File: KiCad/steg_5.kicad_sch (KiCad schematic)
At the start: 12 parts, among them U1 W65C02S, U2 LCD-016N002L

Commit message: Kicad projekt ligger här nu, med alla steg
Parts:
- removed A1: Arduino_Mega2560_R3_Shield, PCM_arduino-library:Arduino_Mega2560_R3_Shield, symbol arduino-library:Arduino_Mega2560_R3_Shield
- removed R1, R2, R3, R4, R5, R6, R7: (no value), symbol Device:R_US
- removed U1: W65C02S, Package_DIP:DIP-40_W15.24mm, symbol 65xx-library:W65C02SxP
- removed U2: LCD-016N002L, Display:LCD-016N002L, symbol Display_Character:LCD-016N002L
- added A3: Mega2560, PCM_arduino-library:Arduino_Mega2560_R3_Shield, symbol arduino-library:Arduino_Mega2560_R3_Shield
- added C5: 100nF, symbol Device:C_Small
- added R15, R16, R17, R18, R19, R20, R21: (no value), symbol Device:R_US
- added U7: W65C02S, Package_DIP:DIP-40_W15.24mm, symbol 65xx-library:W65C02SxP
- added U8: LCD, Display:LCD-016N002L, symbol Display_Character:LCD-016N002L
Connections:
- net +5V: now also C5.1, R15.1, R16.1, R17.1, R18.1, R19.1, R21.1, U7.8 (VDD), U8.2 (VDD)
- net A0: now also A3.A0, U7.9 (A0)
- net A1: now also A3.A1, U7.10 (A1)
- net A10: now also A3.A10, U7.19 (A10)
- net A11: now also A3.A11, U7.20 (A11)
- net A12: now also A3.A12, U7.22 (A12)
- net A13: now also A3.A13, U7.23 (A13)
- net A14: now also A3.A14, U7.24 (A14)
- net A15: now also A3.A15, U7.25 (A15)
- net A2: now also A3.A2, U7.11 (A2)
- net A3: now also A3.A3, U7.12 (A3)
- net A4: now also A3.A4, U7.13 (A4)
- net A5: now also A3.A5, U7.14 (A5)
- net A6: now also A3.A6, U7.15 (A6)
- net A7: now also A3.A7, U7.16 (A7)
- net A8: now also A3.A8, U7.17 (A8)
- net A9: now also A3.A9, U7.18 (A9)
- net D0: now also A3.D22, U7.33 (D0)
- net D1: now also A3.D23, U7.32 (D1)
- net D2: now also A3.D24, U7.31 (D2)
- net D3: now also A3.D25, U7.30 (D3)
- net D4: now also A3.D26, U7.29 (D4)
- net D5: now also A3.D27, U7.28 (D5)
- net D6: now also A3.D28, U7.27 (D6)
- net D7: now also A3.D29, U7.26 (D7)
- net DB4: now also A3.D10, U8.11 (DB4)
- net DB5: now also A3.D9, U8.12 (DB5)
- net DB6: now also A3.D8, U8.13 (DB6)
- net DB7: now also A3.D7, U8.14 (DB7)
- net Earth: now also A3.GND6 (GND), C5.2, R20.2, U7.21 (VSS), U8.1 (VSS), U8.16 (K), U8.5 (R/~{W})
- net at BTN1.1: now also A3.D11
- net at BTN2.1: now also A3.D12
- new net: R16.2, U7.36 (BE)
- new net: A3.D13, U7.7 (SYNC)
- new net: A3.D2 (D2_INT0), U7.37 (ϕ0)
- new net: A3.D3 (D3_INT1), U7.34 (R/~{W})
- new net: A3.D4, U7.40 (~{RES})
- new net: A3.D5, U8.4 (RS)
- new net: A3.D6, U8.6 (E)
- new net: R21.2, U8.15 (A/VEE)
- new net: R20.1, U8.3 (VO)
- new net: R17.2, U7.2 (RDY)
- new net: R18.2, U7.6 (~{NMI})
- new net: R15.2, U7.38 (~{SO})
- new net: R19.2, U7.4 (~{IRQ})

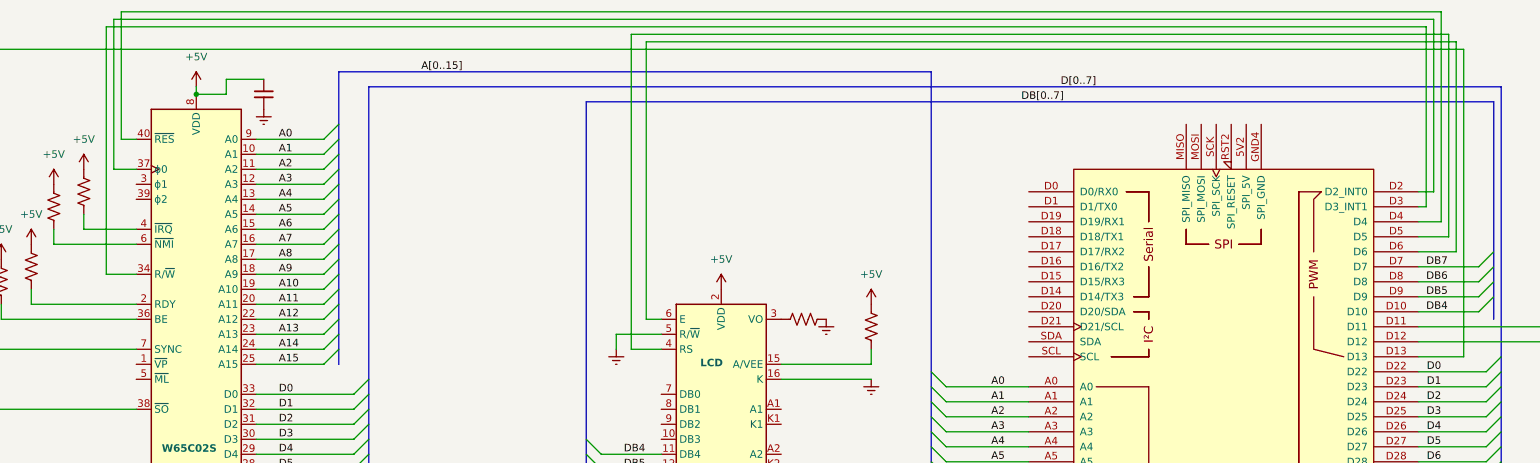
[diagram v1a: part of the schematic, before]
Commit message: Add trim potentiometer symbol and update power symbols in schematics
- Introduced a new trim potentiometer symbol (Device:R_Potentiometer_Trim) with properties for reference, value, footprint, and simulation details.
- Updated existing power symbols for +5V and Earth, including new references and descriptions.
- Adjusted positions and properties of various components in the schematic to enhance clarity and organization.
- Updated multiple schematic images to reflect the latest changes.
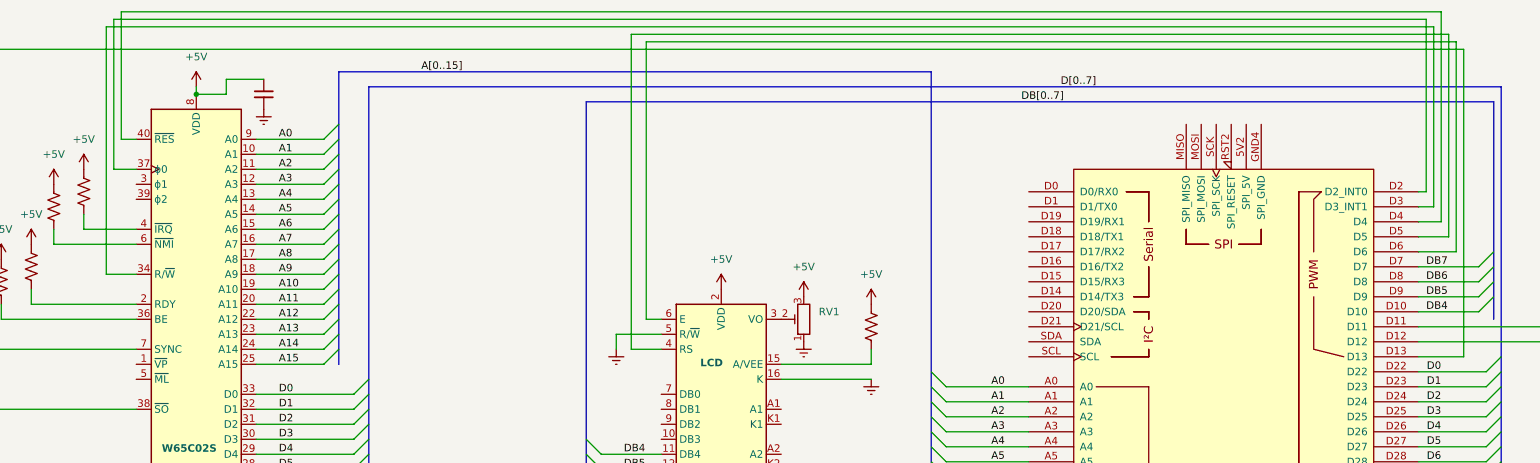
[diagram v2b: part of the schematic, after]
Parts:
- removed R20: (no value), symbol Device:R_US
- added RV1: R_Potentiometer_Trim, symbol Device:R_Potentiometer_Trim
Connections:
- net +5V: now also RV1.3
- net Earth: now also RV1.1
- net at U8.3 (VO): now also RV1.2
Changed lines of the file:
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@@
 	(wire
 		(pts
-			(xy 106.68 67.31) (xy 330.2 67.31)
+			(xy 106.68 67.31) (xy 331.47 67.31)
 		)
 		(stroke
@@
 	(wire
 		(pts
-			(xy 331.47 66.04) (xy 331.47 95.25)
+			(xy 330.2 66.04) (xy 330.2 95.25)
 		)
 		(stroke
@@
 	(wire
 		(pts
-			(xy 331.47 95.25) (xy 328.93 95.25)
+			(xy 330.2 95.25) (xy 328.93 95.25)
 		)
 		(stroke
@@
 	(wire
 		(pts
-			(xy 330.2 97.79) (xy 328.93 97.79)
+			(xy 331.47 97.79) (xy 328.93 97.79)
 		)
 		(stroke
@@
 	(wire
 		(pts
-			(xy 330.2 67.31) (xy 330.2 97.79)
+			(xy 331.47 67.31) (xy 331.47 97.79)
 		)
 		(stroke
@@
 	(wire
 		(pts
-			(xy 107.95 66.04) (xy 331.47 66.04)
+			(xy 107.95 66.04) (xy 330.2 66.04)
 		)
 		(stroke
@@
 	)
 	(symbol
+		(lib_id "power:+5V")
+		(at 224.79 113.03 0)
+		(unit 1)
+		(body_style 1)
+		(exclude_from_sim no)
+		(in_bom yes)
+		(on_board yes)
+		(in_pos_files yes)
+		(dnp no)
+		(fields_autoplaced yes)
+		(property "Reference" "#PWR058"
+			(at 224.79 116.84 0)
+			(hide yes)
+			(show_name no)
+			(do_not_autoplace no)
+			(effects
+				(font
+					(size 1.27 1.27)
+				)
+			)
+		)
+		(property "Value" "+5V"
+			(at 224.79 107.95 0)
+			(show_name no)
+			(do_not_autoplace no)
+			(effects
+				(font
+					(size 1.27 1.27)
+				)
+			)
+		)
+		(property "Footprint" ""
+			(at 224.79 113.03 0)
+			(hide yes)
+			(show_name no)
+			(do_not_autoplace no)
+			(effects
+				(font
+					(size 1.27 1.27)
+				)
+			)
+		)
+		(property "Datasheet" ""
+			(at 224.79 113.03 0)
+			(hide yes)
+			(show_name no)
+			(do_not_autoplace no)
+			(effects
+				(font
+					(size 1.27 1.27)
+				)
+			)
+		)
+		(property "Description" "Power symbol creates a global label with name \"+5V\""
+			(at 224.79 113.03 0)
+			(hide yes)
+			(show_name no)
+			(do_not_autoplace no)
+			(effects
+				(font
+					(size 1.27 1.27)
+				)
+			)
+		)
+		(pin "1"
+		)
+		(instances
+			(project "6502.smutje.se"
+				(path "/34693de8-e0e2-47e7-9988-a0d185b88162"
+					(reference "#PWR058")
+					(unit 1)
+				)
+			)
+		)
+	)
+	(symbol
 		(lib_id "Device:R_US")
 		(at 88.9 110.49 0)
@@
 	)
 	(symbol
+		(lib_id "power:Earth")
+		(at 224.79 120.65 0)
+		(unit 1)
+		(body_style 1)
+		(exclude_from_sim no)
+		(in_bom yes)
+		(on_board yes)
+		(in_pos_files yes)
+		(dnp no)
+		(fields_autoplaced yes)
+		(property "Reference" "#PWR057"
+			(at 224.79 127 0)
+			(hide yes)
+			(show_name no)
+			(do_not_autoplace no)
+			(effects
+				(font
+					(size 1.27 1.27)
+				)
+			)
+		)
+		(property "Value" "Earth"
+			(at 224.79 125.73 0)
+			(hide yes)
+			(show_name no)
+			(do_not_autoplace no)
+			(effects
+				(font
+					(size 1.27 1.27)
+				)
+			)
+		)
+		(property "Footprint" ""
+			(at 224.79 120.65 0)
+			(hide yes)
+			(show_name no)
+			(do_not_autoplace no)
+			(effects
+				(font
+					(size 1.27 1.27)
+				)
+			)
+		)
+		(property "Datasheet" ""
+			(at 224.79 120.65 0)
+			(hide yes)
+			(show_name no)
+			(do_not_autoplace no)
+			(effects
+				(font
+					(size 1.27 1.27)
+				)
+			)
+		)
+		(property "Description" "Power symbol creates a global label with name \"Earth\""
+			(at 224.79 120.65 0)
+			(hide yes)
+			(show_name no)
+			(do_not_autoplace no)
+			(effects
+				(font
+					(size 1.27 1.27)
+				)
+			)
+		)
+		(pin "1"
+		)
+		(instances
+			(project "6502.smutje.se"
+				(path "/34693de8-e0e2-47e7-9988-a0d185b88162"
+					(reference "#PWR057")
+					(unit 1)
+				)
+			)
+		)
+	)
+	(symbol
 		(lib_id "Device:R_US")
 		(at 97.79 97.79 0)
@@
 	)
 	(symbol
-		(lib_id "power:Earth")
-		(at 228.6 116.84 0)
+		(lib_id "Device:R_Potentiometer_Trim")
+		(at 224.79 116.84 180)
 		(unit 1)
 		(body_style 1)
@@
 		(dnp no)
 		(fields_autoplaced yes)
-		(property "Reference" "#PWR049"
-			(at 228.6 123.19 0)
-			(hide yes)
+		(property "Reference" "RV1"
+			(at 227.33 115.5699 0)
 			(show_name no)
 			(do_not_autoplace no)
@@
 					(size 1.27 1.27)
 				)
+				(justify right)
 			)
 		)
-		(property "Value" "Earth"
-			(at 228.6 121.92 0)
+		(property "Value" "R_Potentiometer_Trim"
+			(at 227.33 118.1099 0)
 			(hide yes)
 			(show_name no)
@@
 					(size 1.27 1.27)
 				)
+				(justify right)
 			)
 		)
 		(property "Footprint" ""
-			(at 228.6 116.84 0)
+			(at 224.79 116.84 0)
 			(hide yes)
 			(show_name no)
@@
 		)
 		(property "Datasheet" ""
-			(at 228.6 116.84 0)
+			(at 224.79 116.84 0)
 			(hide yes)
 			(show_name no)
@@
 			)
 		)
-		(property "Description" "Power symbol creates a global label with name \"Earth\""
-			(at 228.6 116.84 0)
+		(property "Description" "Trim-potentiometer"
+			(at 224.79 116.84 0)
+			(hide yes)
+			(show_name no)
+			(do_not_autoplace no)
+			(effects
+				(font
+					(size 1.27 1.27)
+				)
+			)
+		)
+		(property "Sim.Device" "R"
+			(at 224.79 116.84 0)
 			(hide yes)
 			(show_name no)
@@
 			)
 		)
+		(property "Sim.Type" "POT"
+			(at 224.79 116.84 0)
+			(hide yes)
+			(show_name no)
+			(do_not_autoplace no)
+			(effects
+				(font
+					(size 1.27 1.27)
+				)
+			)
+		)
+		(property "Sim.Pins" "1=r0 2=wiper 3=r1"
+			(at 224.79 116.84 0)
+			(hide yes)
+			(show_name no)
+			(do_not_autoplace no)
+			(effects
+				(font
+					(size 1.27 1.27)
+				)
+			)
+		)
+		(pin "3"
+		)
+		(pin "2"
+		)
 		(pin "1"
 		)
@@
 			(project "6502.smutje.se"
 				(path "/34693de8-e0e2-47e7-9988-a0d185b88162"
-					(reference "#PWR049")
+					(reference "RV1")
 					(unit 1)
 				)
@@
 					(unit 1)
 				)
-			)
-		)
-	)
-	(symbol
-		(lib_id "Device:R_US")
-		(at 224.79 116.84 90)
-		(unit 1)
-		(body_style 1)
-		(exclude_from_sim no)
-		(in_bom yes)
-		(on_board yes)
-		(in_pos_files yes)
-		(dnp no)
-		(property "Reference" "R20"
-			(at 223.5199 114.3 90)
-			(hide yes)
-			(show_name no)
-			(do_not_autoplace no)
-			(effects
-				(font
-					(size 1.27 1.27)
-				)
-				(justify left)
-			)
-		)
-		(property "Value" ""
-			(at 226.0599 114.3 0)
-			(show_name no)
-			(do_not_autoplace no)
-			(effects
-				(font
-					(size 1.27 1.27)
-				)
-				(justify left)
-			)
-		)
-		(property "Footprint" ""
-			(at 225.044 115.824 90)
-			(hide yes)
-			(show_name no)
-			(do_not_autoplace no)
-			(effects
-				(font
-					(size 1.27 1.27)
-				)
-			)
-		)
-		(property "Datasheet" ""
-			(at 224.79 116.84 0)
-			(hide yes)
-			(show_name no)
-			(do_not_autoplace no)
-			(effects
-				(font
-					(size 1.27 1.27)
-				)
-			)
-		)
-		(property "Description" "Resistor, US symbol"
-			(at 224.79 116.84 0)
-			(hide yes)
-			(show_name no)
-			(do_not_autoplace no)
-			(effects
-				(font
-					(size 1.27 1.27)
-				)
-			)
-		)
-		(pin "1"
-		)
-		(pin "2"
-		)
-		(instances
-			(project "6502.smutje.se"
-				(path "/34693de8-e0e2-47e7-9988-a0d185b88162"
-					(reference "R20")
-					(unit 1)
-				)

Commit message: Revert "Add trim potentiometer symbol and update power symbols in schematics"
This reverts commit c4bb345892a428583a00d61d4c040ffcc3a1eb40.
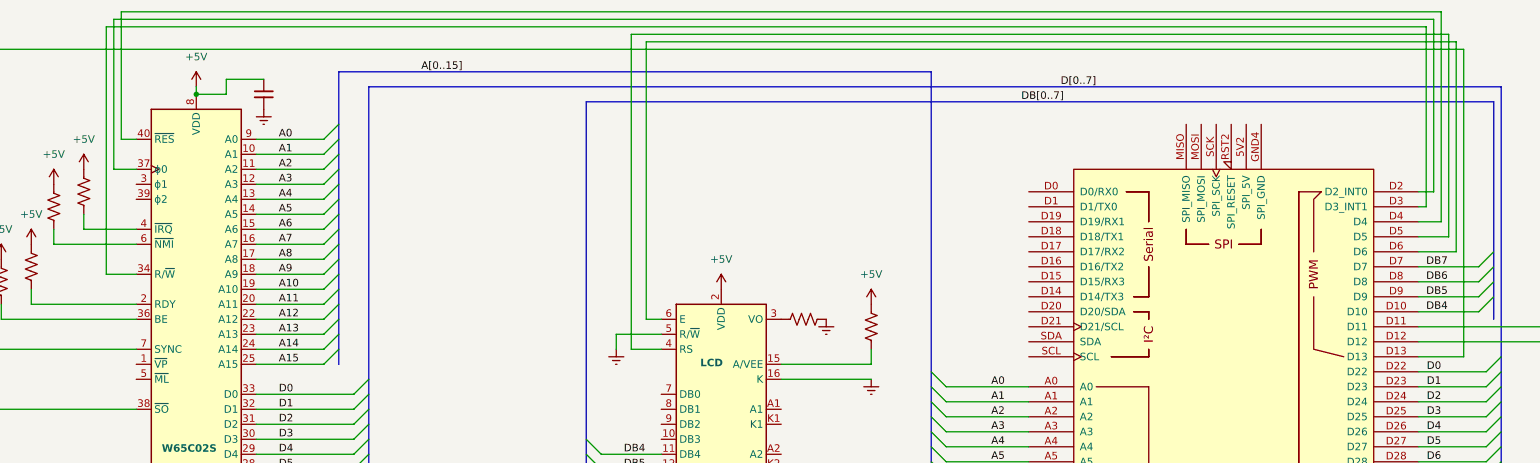
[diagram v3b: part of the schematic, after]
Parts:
- removed RV1: R_Potentiometer_Trim, symbol Device:R_Potentiometer_Trim
- added R20: (no value), symbol Device:R_US
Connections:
- net Earth: now also R20.2
- net at U8.3 (VO): now also R20.1
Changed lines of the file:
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@@
 	(wire
 		(pts
-			(xy 106.68 67.31) (xy 331.47 67.31)
+			(xy 106.68 67.31) (xy 330.2 67.31)
 		)
 		(stroke
@@
 	(wire
 		(pts
-			(xy 330.2 66.04) (xy 330.2 95.25)
+			(xy 331.47 66.04) (xy 331.47 95.25)
 		)
 		(stroke
@@
 	(wire
 		(pts
-			(xy 330.2 95.25) (xy 328.93 95.25)
+			(xy 331.47 95.25) (xy 328.93 95.25)
 		)
 		(stroke
@@
 	(wire
 		(pts
-			(xy 331.47 97.79) (xy 328.93 97.79)
+			(xy 330.2 97.79) (xy 328.93 97.79)
 		)
 		(stroke
@@
 	(wire
 		(pts
-			(xy 331.47 67.31) (xy 331.47 97.79)
+			(xy 330.2 67.31) (xy 330.2 97.79)
 		)
 		(stroke
@@
 	(wire
 		(pts
-			(xy 107.95 66.04) (xy 330.2 66.04)
+			(xy 107.95 66.04) (xy 331.47 66.04)
 		)
 		(stroke
@@
 	)
 	(symbol
-		(lib_id "power:+5V")
-		(at 224.79 113.03 0)
-		(unit 1)
-		(body_style 1)
-		(exclude_from_sim no)
-		(in_bom yes)
-		(on_board yes)
-		(in_pos_files yes)
-		(dnp no)
-		(fields_autoplaced yes)
-		(property "Reference" "#PWR058"
-			(at 224.79 116.84 0)
-			(hide yes)
-			(show_name no)
-			(do_not_autoplace no)
-			(effects
-				(font
-					(size 1.27 1.27)
-				)
-			)
-		)
-		(property "Value" "+5V"
-			(at 224.79 107.95 0)
-			(show_name no)
-			(do_not_autoplace no)
-			(effects
-				(font
-					(size 1.27 1.27)
-				)
-			)
-		)
-		(property "Footprint" ""
-			(at 224.79 113.03 0)
-			(hide yes)
-			(show_name no)
-			(do_not_autoplace no)
-			(effects
-				(font
-					(size 1.27 1.27)
-				)
-			)
-		)
-		(property "Datasheet" ""
-			(at 224.79 113.03 0)
-			(hide yes)
-			(show_name no)
-			(do_not_autoplace no)
-			(effects
-				(font
-					(size 1.27 1.27)
-				)
-			)
-		)
-		(property "Description" "Power symbol creates a global label with name \"+5V\""
-			(at 224.79 113.03 0)
-			(hide yes)
-			(show_name no)
-			(do_not_autoplace no)
-			(effects
-				(font
-					(size 1.27 1.27)
-				)
-			)
-		)
-		(pin "1"
-		)
-		(instances
-			(project "6502.smutje.se"
-				(path "/34693de8-e0e2-47e7-9988-a0d185b88162"
-					(reference "#PWR058")
-					(unit 1)
-				)
-			)
-		)
-	)
-	(symbol
 		(lib_id "Device:R_US")
 		(at 88.9 110.49 0)
@@
 	)
 	(symbol
-		(lib_id "power:Earth")
-		(at 224.79 120.65 0)
-		(unit 1)
-		(body_style 1)
-		(exclude_from_sim no)
-		(in_bom yes)
-		(on_board yes)
-		(in_pos_files yes)
-		(dnp no)
-		(fields_autoplaced yes)
-		(property "Reference" "#PWR057"
-			(at 224.79 127 0)
-			(hide yes)
-			(show_name no)
-			(do_not_autoplace no)
-			(effects
-				(font
-					(size 1.27 1.27)
-				)
-			)
-		)
-		(property "Value" "Earth"
-			(at 224.79 125.73 0)
-			(hide yes)
-			(show_name no)
-			(do_not_autoplace no)
-			(effects
-				(font
-					(size 1.27 1.27)
-				)
-			)
-		)
-		(property "Footprint" ""
-			(at 224.79 120.65 0)
-			(hide yes)
-			(show_name no)
-			(do_not_autoplace no)
-			(effects
-				(font
-					(size 1.27 1.27)
-				)
-			)
-		)
-		(property "Datasheet" ""
-			(at 224.79 120.65 0)
-			(hide yes)
-			(show_name no)
-			(do_not_autoplace no)
-			(effects
-				(font
-					(size 1.27 1.27)
-				)
-			)
-		)
-		(property "Description" "Power symbol creates a global label with name \"Earth\""
-			(at 224.79 120.65 0)
-			(hide yes)
-			(show_name no)
-			(do_not_autoplace no)
-			(effects
-				(font
-					(size 1.27 1.27)
-				)
-			)
-		)
-		(pin "1"
-		)
-		(instances
-			(project "6502.smutje.se"
-				(path "/34693de8-e0e2-47e7-9988-a0d185b88162"
-					(reference "#PWR057")
-					(unit 1)
-				)
-			)
-		)
-	)
-	(symbol
 		(lib_id "Device:R_US")
 		(at 97.79 97.79 0)
@@
 	)
 	(symbol
-		(lib_id "Device:R_Potentiometer_Trim")
-		(at 224.79 116.84 180)
+		(lib_id "power:Earth")
+		(at 228.6 116.84 0)
 		(unit 1)
 		(body_style 1)
@@
 		(dnp no)
 		(fields_autoplaced yes)
-		(property "Reference" "RV1"
-			(at 227.33 115.5699 0)
+		(property "Reference" "#PWR049"
+			(at 228.6 123.19 0)
+			(hide yes)
 			(show_name no)
 			(do_not_autoplace no)
@@
 					(size 1.27 1.27)
 				)
-				(justify right)
 			)
 		)
-		(property "Value" "R_Potentiometer_Trim"
-			(at 227.33 118.1099 0)
+		(property "Value" "Earth"
+			(at 228.6 121.92 0)
 			(hide yes)
 			(show_name no)
@@
 					(size 1.27 1.27)
 				)
-				(justify right)
 			)
 		)
 		(property "Footprint" ""
-			(at 224.79 116.84 0)
+			(at 228.6 116.84 0)
 			(hide yes)
 			(show_name no)
@@
 		)
 		(property "Datasheet" ""
-			(at 224.79 116.84 0)
-			(hide yes)
-			(show_name no)
-			(do_not_autoplace no)
-			(effects
-				(font
-					(size 1.27 1.27)
-				)
-			)
-		)
-		(property "Description" "Trim-potentiometer"
-			(at 224.79 116.84 0)
+			(at 228.6 116.84 0)
 			(hide yes)
 			(show_name no)
@@
 			)
 		)
-		(property "Sim.Device" "R"
-			(at 224.79 116.84 0)
-			(hide yes)
-			(show_name no)
-			(do_not_autoplace no)
-			(effects
-				(font
-					(size 1.27 1.27)
-				)
-			)
-		)
-		(property "Sim.Type" "POT"
-			(at 224.79 116.84 0)
-			(hide yes)
-			(show_name no)
-			(do_not_autoplace no)
-			(effects
-				(font
-					(size 1.27 1.27)
-				)
-			)
-		)
-		(property "Sim.Pins" "1=r0 2=wiper 3=r1"
-			(at 224.79 116.84 0)
+		(property "Description" "Power symbol creates a global label with name \"Earth\""
+			(at 228.6 116.84 0)
 			(hide yes)
 			(show_name no)
@@
 			)
 		)
-		(pin "3"
-		)
-		(pin "2"
-		)
 		(pin "1"
 		)
@@
 			(project "6502.smutje.se"
 				(path "/34693de8-e0e2-47e7-9988-a0d185b88162"
-					(reference "RV1")
+					(reference "#PWR049")
 					(unit 1)
 				)
@@
 					(unit 1)
 				)
+			)
+		)
+	)
+	(symbol
+		(lib_id "Device:R_US")
+		(at 224.79 116.84 90)
+		(unit 1)
+		(body_style 1)
+		(exclude_from_sim no)
+		(in_bom yes)
+		(on_board yes)
+		(in_pos_files yes)
+		(dnp no)
+		(property "Reference" "R20"
+			(at 223.5199 114.3 90)
+			(hide yes)
+			(show_name no)
+			(do_not_autoplace no)
+			(effects
+				(font
+					(size 1.27 1.27)
+				)
+				(justify left)
+			)
+		)
+		(property "Value" ""
+			(at 226.0599 114.3 0)
+			(show_name no)
+			(do_not_autoplace no)
+			(effects
+				(font
+					(size 1.27 1.27)
+				)
+				(justify left)
+			)
+		)
+		(property "Footprint" ""
+			(at 225.044 115.824 90)
+			(hide yes)
+			(show_name no)
+			(do_not_autoplace no)
+			(effects
+				(font
+					(size 1.27 1.27)
+				)
+			)
+		)
+		(property "Datasheet" ""
+			(at 224.79 116.84 0)
+			(hide yes)
+			(show_name no)
+			(do_not_autoplace no)
+			(effects
+				(font
+					(size 1.27 1.27)
+				)
+			)
+		)
+		(property "Description" "Resistor, US symbol"
+			(at 224.79 116.84 0)
+			(hide yes)
+			(show_name no)
+			(do_not_autoplace no)
+			(effects
+				(font
+					(size 1.27 1.27)
+				)
+			)
+		)
+		(pin "1"
+		)
+		(pin "2"
+		)
+		(instances
+			(project "6502.smutje.se"
+				(path "/34693de8-e0e2-47e7-9988-a0d185b88162"
+					(reference "R20")
+					(unit 1)
+				)
